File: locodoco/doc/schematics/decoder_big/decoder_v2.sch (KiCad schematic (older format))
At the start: 119 parts, among them IC1 ATMega8/48/88/168/328, K1 CONN_3, K2 CONN_3, K3 CONN_3, P1 CONN_1, P10 CONN_1, P11 CONN_1, P12 CONN_1, P13 CONN_1, P14 CONN_1, P15 CONN_1, P16 CONN_1, P17 CONN_1, P18 CONN_1, P19 CONN_5, P2 CONN_1, P20 CONN_2, P21 CONN_1, P22 CONN_1, P23 CONN_1, P24 CONN_2, P25 CONN_2, P3 CONN_1, P4 CONN_1, P5 CONN_1, P6 CONN_1, P7 CONN_1, P8 CONN_1, P9 CONN_1, Q1 MOSFET_N, Q2 MOSFET_N, U1 7805, U2 LM2574SMD, U3 L6201PS, U4 RFM12, U5 LM257X, U6 ULN2003A, X1 QUARTZCMS4

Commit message: updated the circuit once again...
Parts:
- removed C4: 100n, symbol C
- removed C6: 100µ, symbol CAPAPOL
- removed D1: DIODESCH, symbol DIODESCH
- removed D10, D7, D8, D9: DIODE, symbol DIODE
- removed GS3, GS8, GS9: GS2, symbol GS2
- removed GS?: GS3, symbol GS3
- removed L1: 330µH, symbol INDUCTOR
- removed P18, P21, P22, P23: CONN_1, symbol CONN_1
- removed R1, R16, R2: R, symbol R
- removed R22, R23: 22k, symbol R
- removed R5, R6: 10k, symbol R
- removed U2: LM2574SMD, symbol LM2574SMD
- added C14, C8, C9: 100n, symbol C
- added D1, D2, D3, D4: DIODE, symbol DIODE
- added GS4: GS3, symbol GS3
- added GS5: GS2, symbol GS2
- added P5, P8: CONN_1, symbol CONN_1
- added R18, R20: 10k, symbol R
- added R8: 1k5, symbol R
- added U4: LP2950, symbol 7805
- R1: renamed from R3; value R -> 2k2
- R10: renamed from R15; value R -> 470
- R11: renamed from R10; value 100 -> 220
- R21: value R -> 2k2
- R28: renamed from R26; value R -> 10
- R29: renamed from R27; value R -> 1
- R9: renamed from R14; value R -> 470
- U3: renamed from U1; value 7805 -> 78XX
- renumbered C3 to C1, C16 to C10, C22 to C11, C14 to C12, C17 to C13, C11 to C15, C12 to C16, C13 to C17, C15 to C18, C18 to C19, C1 to C2, C19 to C20, C20 to C21, C21 to C22, C10 to C23, C9 to C24, C7 to C3, C8 to C4, C23 to C5, C2 to C6, C5 to C7, D3 to D5, D4 to D6, D5 to D7, D6 to D8, D2 to D9, GS6 to GS1, GS7 to GS2, GS1 to GS3, GS2 to GS6, K3 to K1, K1 to K2, K2 to K3, L2 to L1, P19 to P1, P2 to P10, P3 to P11, P4 to P12, P6 to P13, P10 to P14, P24 to P15, P5 to P16, P7 to P17, P11 to P18, P25 to P19, P20 to P2, P15 to P20, P16 to P21, P13 to P22, P14 to P23, P8 to P3, P9 to P4, P12 to P6, P17 to P7, P1 to P9, R11 to R12, R31 to R13, R32 to R14, R24 to R15, R33 to R16, R28 to R19, R4 to R2, R20 to R22, R12 to R23, R29 to R24, R18 to R25, R13 to R26, R19 to R27, R34 to R3, R8 to R30, R9 to R31, R25 to R4, R35 to R5, R30 to R6, U3 to U1, U6 to U2, U4 to U5, U5 to U6
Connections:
- net labels added: GND_sep, gnd_fet, miso, rfm_sel, v_fet_gate
- net labels removed: GND_REG5, VCC_REG5, vcc_3.3
- wire segments 384 -> 352
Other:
- note added: "+5V or *V regulator"
- note added: "3.3V supply\n(RFM12B only)"
- note added: "500..1000mA\npower switch\n(optional)"
- note added: "5V logic\n(RFM12 variant)"
- note added: "Servo A (opt.)"
- note added: "Servo B/SUSI\n(opt.)"
- note added: "additional *V or +5V power supply\n(simple variant, optional)"
- note added: "dcc snoop\n(optional)"
- note added: "ext. cap (logic, optional)"
- note added: "ext. cap\n(motor & switching, optional)"
- note added: "high current\nfet driver (optional)"
- note added: "motor free wheeling"
- note added: "rail connector"
- note added: "rail power measurement\n(optional)"
- note added: "sep. GND/rect.\n(opt.)"
- note removed: "3.3V power regulator"
- note removed: "Ext. Cap (Logic)"
- note removed: "Ext. Cap (Motor)"
- note removed: "Power-Switching"
- note removed: "Rail\nConnector"
- note removed: "Servo A"
- note removed: "Servo B/SUSI"
- note removed: "dcc snoop"
- note removed: "power switch 1.23...20 V"
- note removed: "power switching\n(simple variant)"
- note removed: "rail power measurement"
- moved on the sheet: P6, P_RAIL1, R23, R25, R26, R27

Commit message: updated schematic, ++libs
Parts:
- removed Q1, Q2: MOSFET_N, symbol MOSFET_N
- added D14, D15, D18, D5, D6, D7, D8, D9: DIODE, symbol DIODE
- added IC1: IRF8313, symbol IRF83XX
- C11, C23, C24: value C -> 100n
- R4: renamed from R6; value 4k7 -> 22k
- R5: renamed from R4; value 4k7 -> 22k
- renumbered D5 to D10, D6 to D11, D7 to D12, D8 to D13, D9 to D16, GS2 to GS1, GS1 to GS2, IC1 to IC2, R5 to R6
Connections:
- wire segments 352 -> 378
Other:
- note added: "Logic & Motor rectifier\n(alternat. diodes)"
- moved on the sheet: C5, D10, D11, D12, D13, GS1, GS2, P2, R4, R5

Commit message: updated the schematic once again
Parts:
- removed C11, C22, C6, C7, C8, C9: 100n, symbol C
- removed C21: 330n, symbol C
- removed D18, D5, D6, D7, D8, D9: DIODE, symbol DIODE
- removed GS3, GS5, GS6: GS2, symbol GS2
- removed GS4: GS3, symbol GS3
- removed K1, K2, K3: CONN_3, symbol CONN_3
- removed P14, P18, P21, P4, P6, P7, P9: CONN_1, symbol CONN_1
- removed P19: CONN_2, symbol CONN_2
- removed P_IR1: CONN_2X2, symbol CONN_2X2
- removed R10, R9: 470, symbol R
- removed R17: 47k, symbol R
- removed R18, R20: 10k, symbol R
- removed R21: 2k2, symbol R
- removed R28: 10, symbol R
- removed R29: 1, symbol R
- removed R8: 1k5, symbol R
- removed U3: 78XX, symbol 7805
- removed U4: LP2950, symbol 7805
- added P24, P25: CONN_2, symbol CONN_2
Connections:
- net labels added: aref, fsk, mosi, reset, rfm_int, sck
- net labels removed: +3.3V, GND_sep, gpio0
- wire segments 378 -> 307
- no-connect marks 4 -> 5
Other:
- note removed: "3.3V supply\n(RFM12B only)"
- note removed: "5V logic\n(RFM12 variant)"
- note removed: "Logic & Motor rectifier\n(alternat. diodes)"
- note removed: "Servo A (opt.)"
- note removed: "additional *V or +5V power supply\n(simple variant, optional)"
- note removed: "ext. cap (logic, optional)"
- moved on the sheet: P5, P8, R22

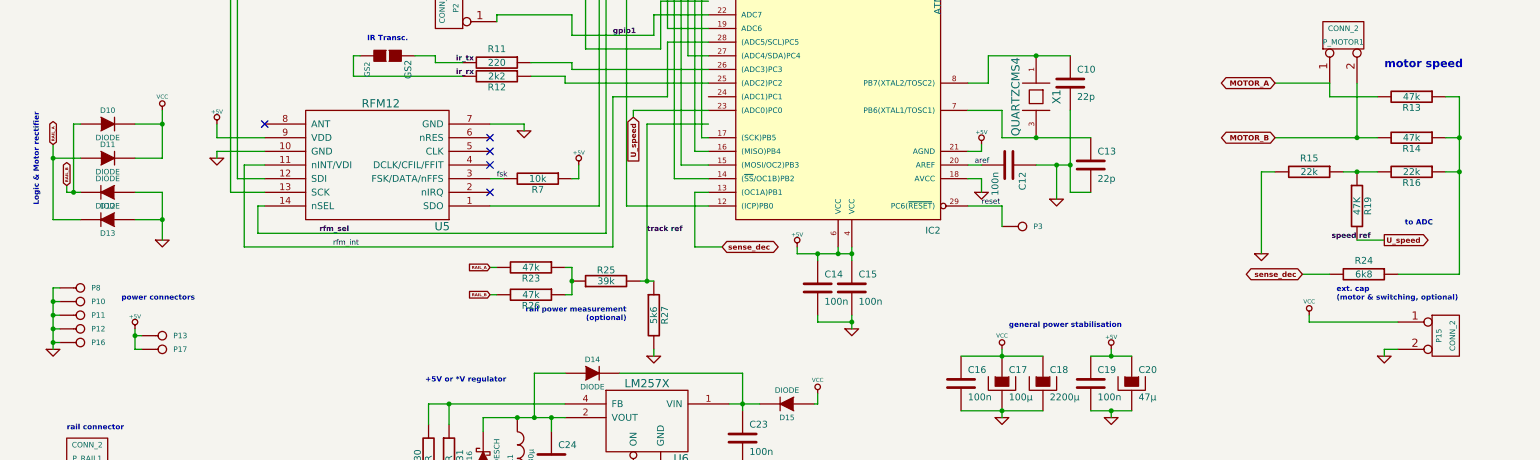
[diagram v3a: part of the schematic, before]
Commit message: bugfix: rfm12 int pin wrong...
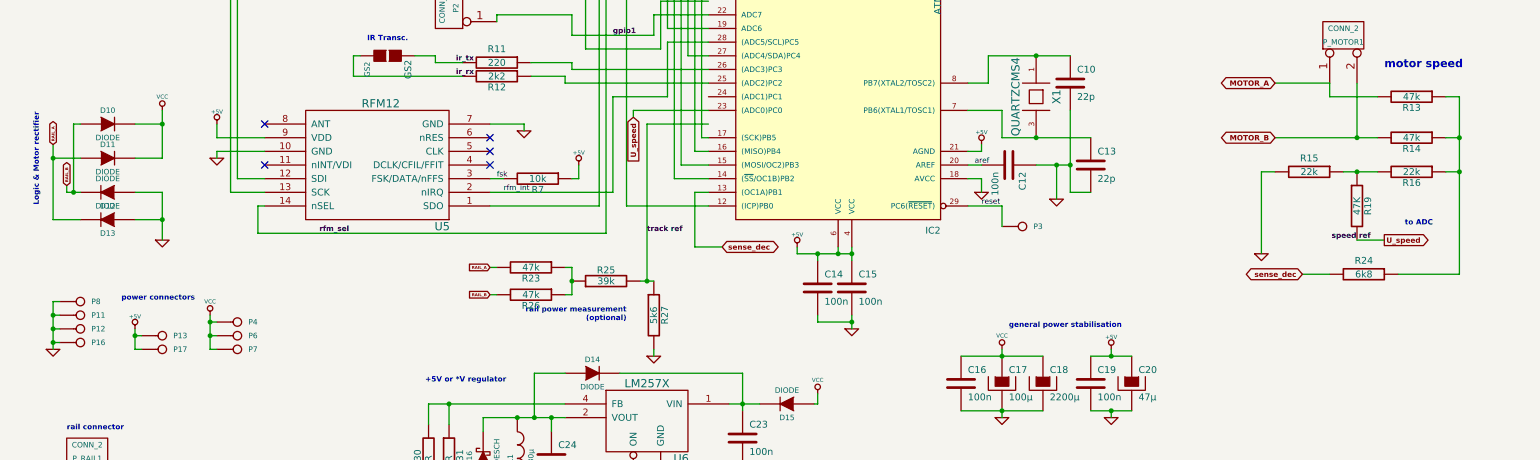
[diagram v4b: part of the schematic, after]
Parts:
- removed P10: CONN_1, symbol CONN_1
- removed P15: CONN_2, symbol CONN_2
- added P4, P6, P7: CONN_1, symbol CONN_1
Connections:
- net VCC: now also P4.1, P6.1, P7.1
- net rfm_int: now also U5.2 (nIRQ); no longer U5.11 (nINT/VDI)
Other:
- note removed: "ext. cap\n(motor & switching, optional)"
- moved on the sheet: P8

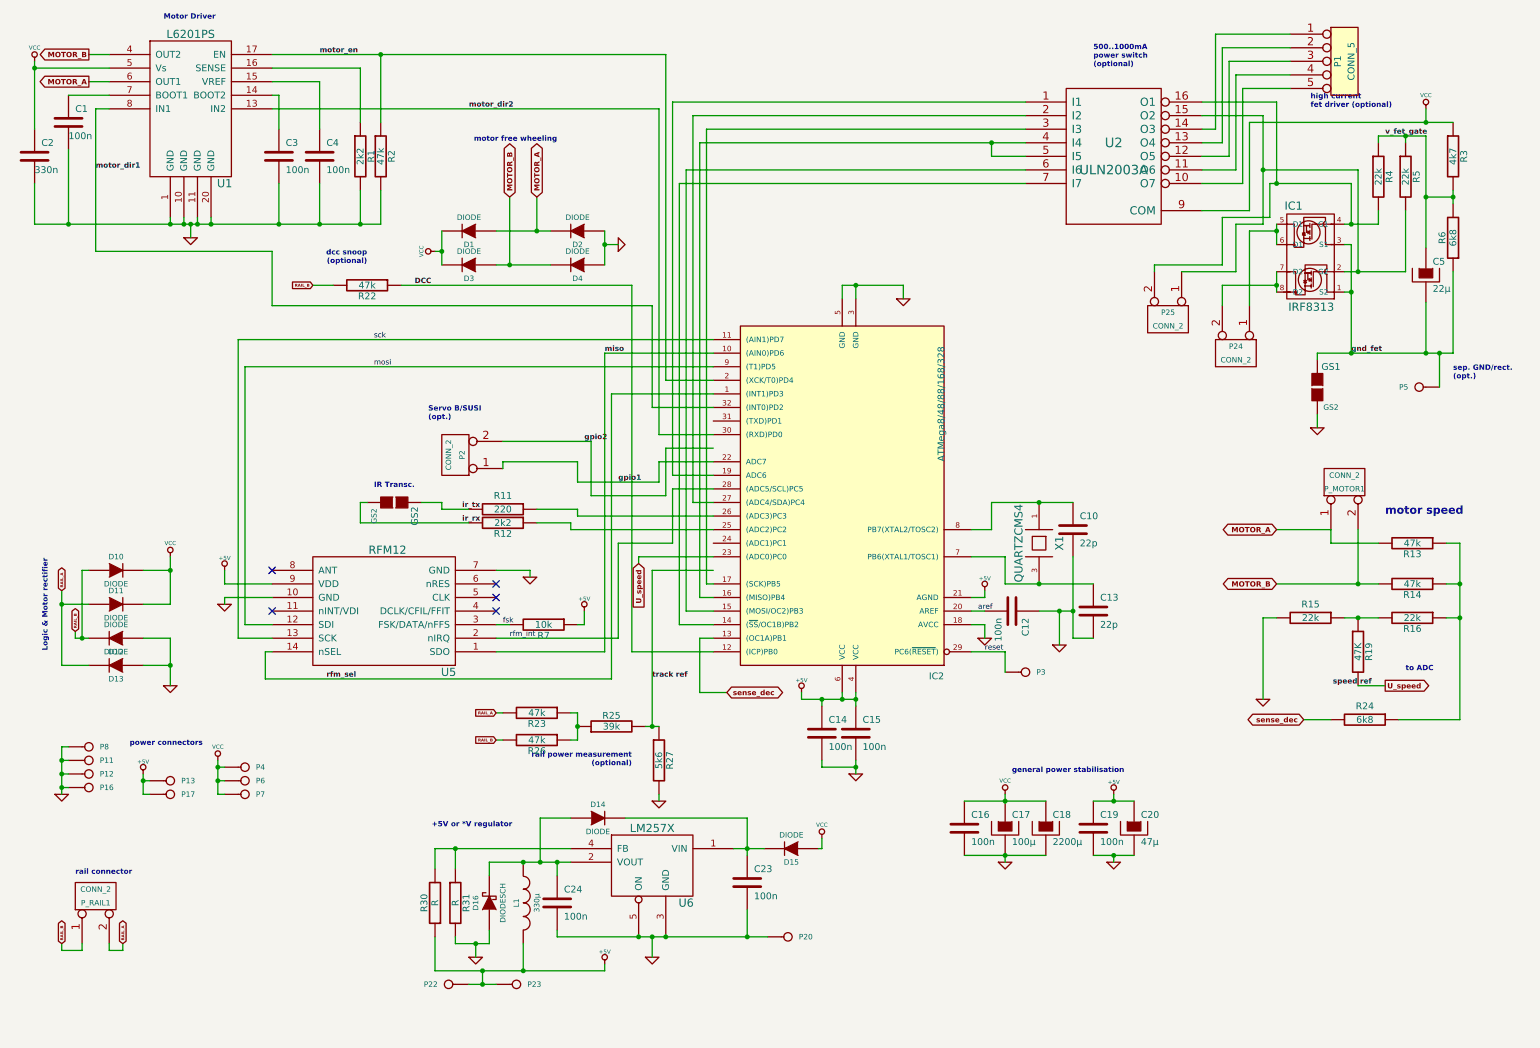
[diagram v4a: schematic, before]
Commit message: had to re-wire stuff for a new version of kicad *sigh*
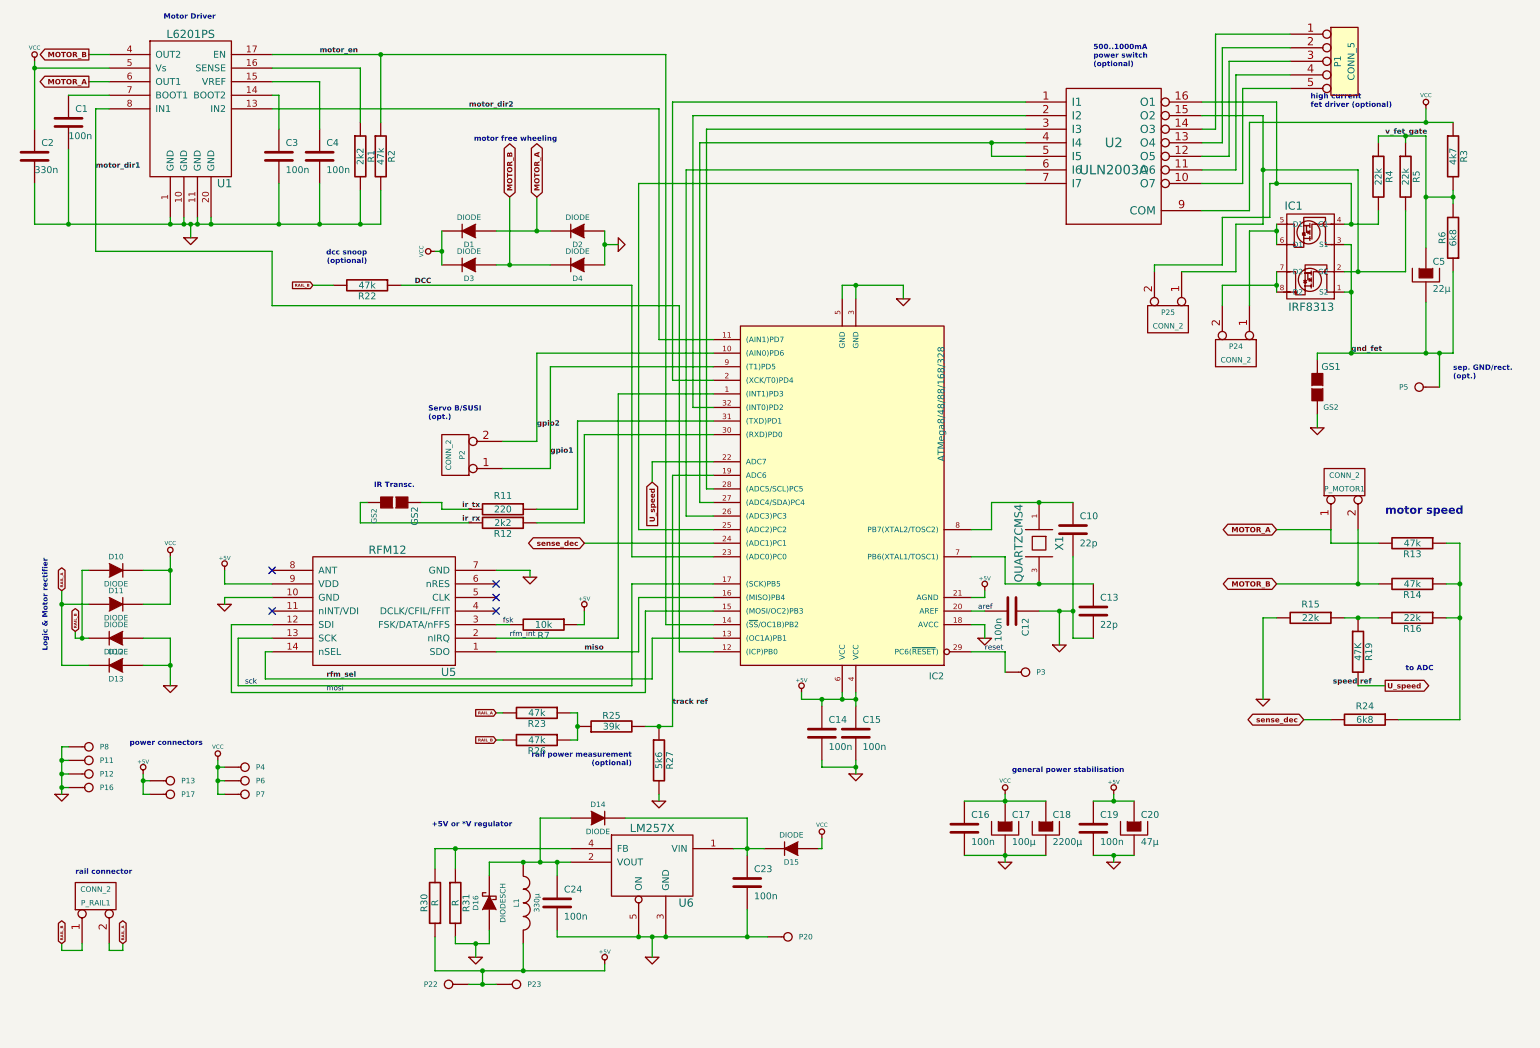
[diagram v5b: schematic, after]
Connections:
- net DCC: now also IC2.23 ((ADC0)PC0); no longer IC2.12 ((ICP)PB0)
- net U_speed: now also IC2.22 (ADC7); no longer IC2.23 ((ADC0)PC0)
- net gpio1: now also IC2.9 ((T1)PD5); no longer IC2.22 (ADC7)
- net gpio2: now also IC2.10 ((AIN0)PD6)
- net miso: now also IC2.16 ((MISO)PB4); no longer IC2.10 ((AIN0)PD6)
- net mosi: now also IC2.15 ((MOSI/OC2)PB3); no longer IC2.9 ((T1)PD5)
- net motor_dir1: now also IC2.12 ((ICP)PB0); no longer IC2.32 ((INT0)PD2)
- net motor_dir2: now also IC2.11 ((AIN1)PD7); no longer IC2.30 ((RXD)PD0)
- net motor_en: now also IC2.14 ((~SS~/OC1B)PB2); no longer IC2.2 ((XCK/T0)PD4)
- net rfm_int: now also IC2.1 ((INT1)PD3); no longer IC2.28 ((ADC5/SCL)PC5)
- net rfm_sel: now also IC2.13 ((OC1A)PB1); no longer IC2.1 ((INT1)PD3)
- net sck: now also IC2.17 ((SCK)PB5); no longer IC2.11 ((AIN1)PD7)
- net sense_dec: now also IC2.24 ((ADC1)PC1); no longer IC2.13 ((OC1A)PB1)
- net track ref: now also IC2.19 (ADC6)
- net at R11.1: now also IC2.31 ((TXD)PD1); no longer IC2.26 ((ADC3)PC3)
- net at R12.1: now also IC2.30 ((RXD)PD0); no longer IC2.25 ((ADC2)PC2)
- net at U2.1 (I1): now also IC2.2 ((XCK/T0)PD4); no longer IC2.19 (ADC6)
- net at U2.2 (I2): now also IC2.32 ((INT0)PD2); no longer IC2.27 ((ADC4/SDA)PC4)
- net at U2.3 (I3): now also IC2.28 ((ADC5/SCL)PC5); no longer IC2.17 ((SCK)PB5)
- net at U2.4 (I4), U2.5 (I5): now also IC2.27 ((ADC4/SDA)PC4); no longer IC2.16 ((MISO)PB4)
- net at U2.6 (I6): now also IC2.26 ((ADC3)PC3); no longer IC2.15 ((MOSI/OC2)PB3)
- net at U2.7 (I7): now also IC2.25 ((ADC2)PC2); no longer IC2.14 ((~SS~/OC1B)PB2)

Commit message: blah - minor fixes...
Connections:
- net +5V: now also IC2.18 (AVCC); no longer IC2.21 (AGND)
- net GND: now also IC2.21 (AGND); no longer IC2.18 (AVCC)
- net gpio1: now also IC2.10 ((AIN0)PD6), P2.2 (PM); no longer IC2.9 ((T1)PD5), P2.1 (P1)
- net gpio2: now also IC2.9 ((T1)PD5), P2.1 (P1); no longer IC2.10 ((AIN0)PD6), P2.2 (PM)
- net gpo4b: now reaches IC1.2 (G2), P25.1 (P1), R5.2, U2.15 (O2)
- net gpo3b: now reaches IC1.4 (G1), P25.2 (PM), R4.2, U2.16 (O1)
- net gpo9: now reaches P1.5, U2.10 (O7)
- net gpo8: now reaches P1.4, U2.11 (O6)
- net gpo7: now reaches P1.3, U2.12 (O5)
- net gpo6: now reaches P1.2, U2.13 (O4)
- net gpo5: now reaches P1.1, U2.14 (O3)
- net gpo3a: now reaches IC1.5 (D1), IC1.6 (D1), P24.1 (P1)
- net gpo4a: now reaches IC1.7 (D2), IC1.8 (D2), P24.2 (PM)
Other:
- moved on the sheet: C16, C17, C18, C19, C20, P_MOTOR1, R13, R14, R15, R16, R19, R24
